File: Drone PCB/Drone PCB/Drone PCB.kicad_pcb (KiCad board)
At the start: 2 copper layers, 94 x 94 mm, 44 parts, among them J1 Conn_01x02_Socket, J2 Conn_01x02_Socket, J3 Conn_01x02_Socket, J4 Conn_01x02_Socket, J5 Conn_01x02_Socket, J6 Conn_01x02_Socket, J7 Conn_01x06_Pin, J8 Conn_01x06_Socket, Q1 SI2302, Q2 SI2302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

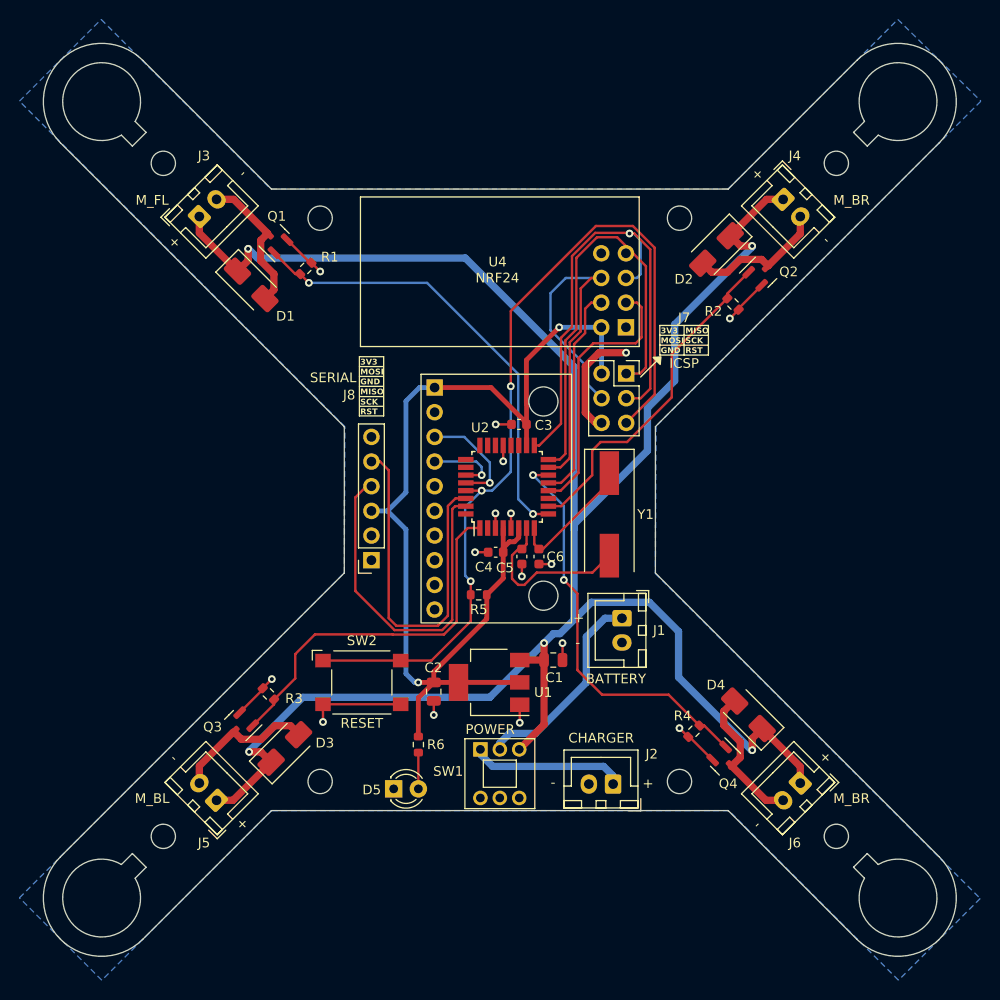
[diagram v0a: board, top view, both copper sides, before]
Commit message: PCB layout improved
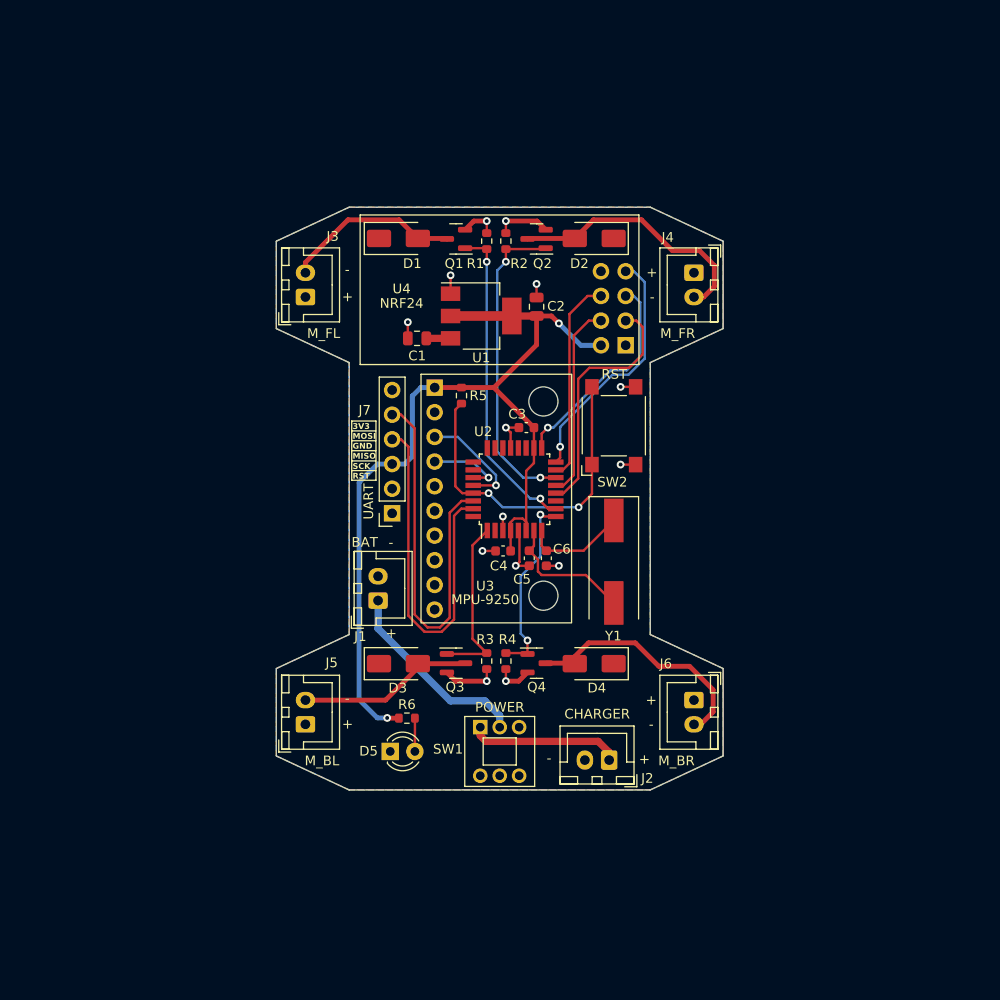
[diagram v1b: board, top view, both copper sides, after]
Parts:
- removed the J7 at (13.0, -12.9)
- removed REF** (x8): MountingHole_2.5mm, MountingHole:MountingHole_2.5mm
- moved C2 41.0 mm to (3.79, -19.8), turned to 90 degrees
- moved U1 37.7 mm to (-1.91, -18.8), turned to 0 degrees
- moved SW2 37.0 mm to (11.8, -7.50), turned to 90 degrees
- moved C1 36.0 mm to (-8.51, -16.5), turned to 180 degrees
- moved J1 25.2 mm to (-12.5, 10.5), turned to 90 degrees
- moved R2 24.3 mm to (0.64, -26.5), turned to 90 degrees
- moved Q2 23.4 mm to (3.80, -26.7), turned to 180 degrees
- moved Q3 23.2 mm to (-4.50, 16.9), turned to 0 degrees
- moved R3 22.7 mm to (-1.34, 16.7), turned to -90 degrees
- moved Q4 21.9 mm to (3.80, 16.9), turned to 0 degrees
- moved R4 20.7 mm to (0.64, 16.7), turned to -90 degrees
- moved R5 20.6 mm to (-3.94, -10.6), turned to -90 degrees
- moved R1 18.8 mm to (-1.34, -26.5), turned to 90 degrees
- moved Q1 18.7 mm to (-4.50, -26.7), turned to 180 degrees
- moved D4 16.7 mm to (9.73, 17.0), turned to 180 degrees
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- renumbered J8 to J7
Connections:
- U2 pad 10: MOTOR_FR -> MOTOR_FL
- U2 pad 14: MOTOR_BR -> MOTOR_FR
- U2 pad 9: MOTOR_FL -> MOTOR_BR
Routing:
- net VCC: track 222.7 -> 2.50 mm, vias 5 -> 0
- net RESET: track 91.9 -> 35.3 mm, vias 3 -> 2
- net SCK: track 55.0 -> 22.3 mm
- net MOTOR_BR: track 41.7 -> 19.4 mm
- net MOSI: track 41.9 -> 21.1 mm
- net MOTOR_BL: track 38.6 -> 18.0 mm
- net MISO: track 45.1 -> 25.7 mm, vias 0 -> 1
- net GND: track 55.6 -> 40.1 mm, vias 16 -> 14
- net MOTOR_FL: track 47.0 -> 33.0 mm
- net +3V3: track 109.7 -> 97.2 mm
- net Net-(D2-A): track 14.4 -> 26.7 mm
- net Net-(D4-A): track 15.0 -> 25.4 mm
- net Net-(U2-XTAL2/PB7): track 14.8 -> 10.5 mm
- net Net-(U2-XTAL1/PB6): track 17.6 -> 13.9 mm
- net Net-(D1-A): track 14.7 -> 18.3 mm
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- added copper zone on F.Cu, net VCC
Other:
- board size 94 x 94 mm -> 46 x 60 mm

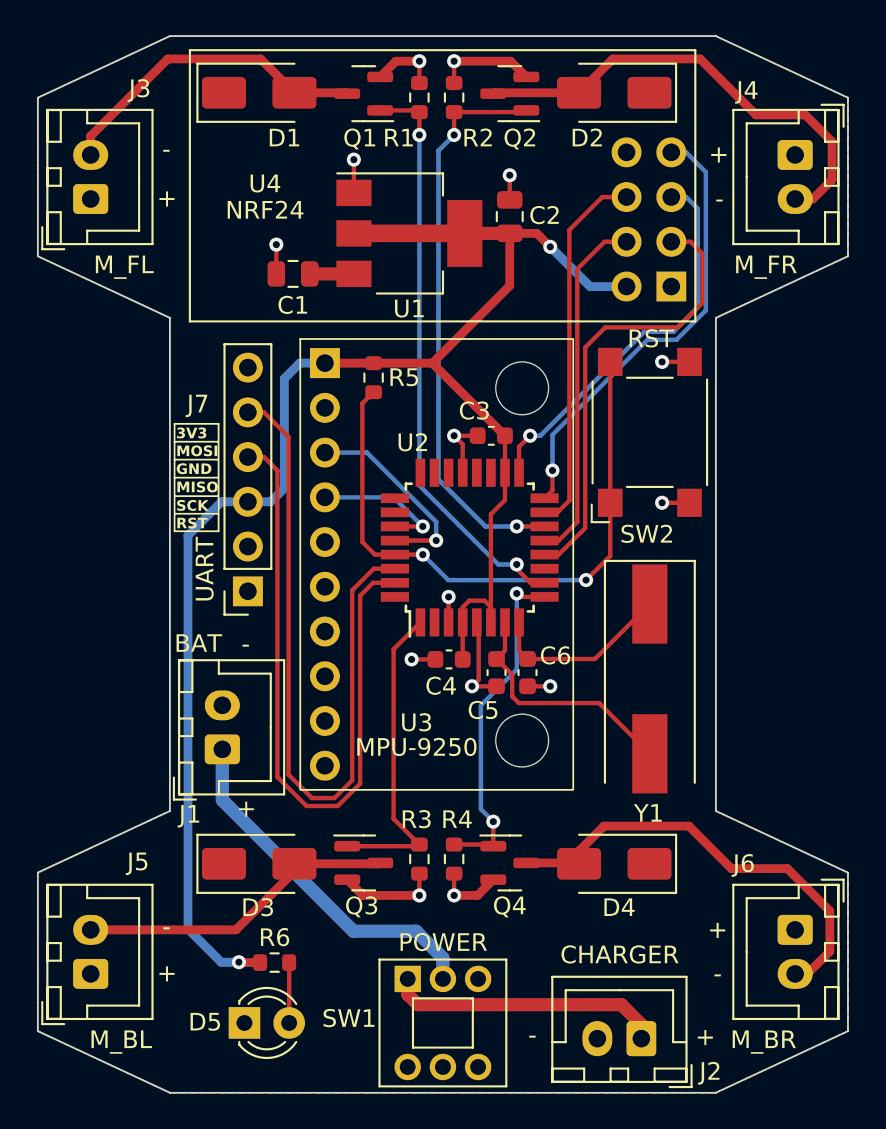
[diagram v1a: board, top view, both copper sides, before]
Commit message: 3D model finished
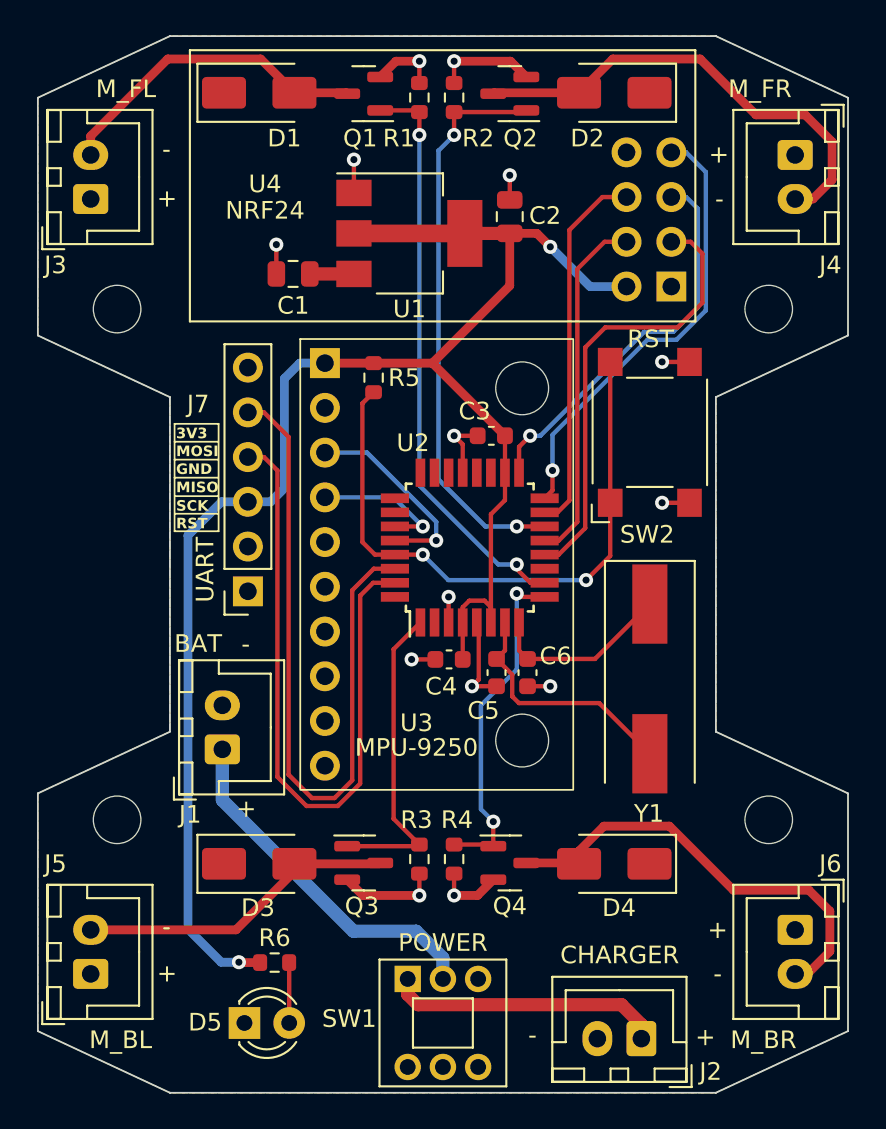
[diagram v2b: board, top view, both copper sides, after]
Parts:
- added REF**: MountingHole_2.7mm_M2.5, MountingHole:MountingHole_2.7mm_M2.5, F.Cu at (18.5, -14.5)
- added REF**: MountingHole_2.7mm_M2.5, MountingHole:MountingHole_2.7mm_M2.5, F.Cu at (-18.5, -14.5)
- added REF**: MountingHole_2.7mm_M2.5, MountingHole:MountingHole_2.7mm_M2.5, F.Cu at (18.5, 14.5)
- added REF**: MountingHole_2.7mm_M2.5, MountingHole:MountingHole_2.7mm_M2.5, F.Cu at (-18.5, 14.5)
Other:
- outline, holes or cut-outs redrawn

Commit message: Images included
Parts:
- moved C2 176.6 mm to (151.4, 77.3)
- moved C3 176.6 mm to (150.3, 89.7)
- moved C4 176.6 mm to (147.9, 102.4)
- moved D5 176.6 mm to (136.3, 123.0)
- moved J1 176.6 mm to (135.0, 107.5)
- moved J7 176.6 mm to (136.5, 98.5)
- moved R5 176.6 mm to (143.6, 86.4)
- moved R6 176.6 mm to (138.0, 119.6)
- moved C1 176.6 mm to (139.1, 80.5)
- moved C5 176.6 mm to (150.6, 103.2)
- moved C6 176.6 mm to (152.4, 103.2)
- moved D1 176.6 mm to (137.1, 70.2)
- moved D2 176.6 mm to (157.3, 70.2)
- moved D3 176.6 mm to (137.1, 114.0)
- moved D4 176.6 mm to (157.3, 114.0)
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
